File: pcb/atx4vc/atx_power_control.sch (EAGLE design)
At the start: 59 parts, among them IC2 REG1117, IC3 STM32F042F4, IC4 MY_7905DT, J1 ATX24RH, SW1 324_SW, SW2 324_SW, SW3 324_SW, SW4 324_SW, SW5 324_SW, SW7 324_SW, U1 USBC_16P, U2 USBC_16P

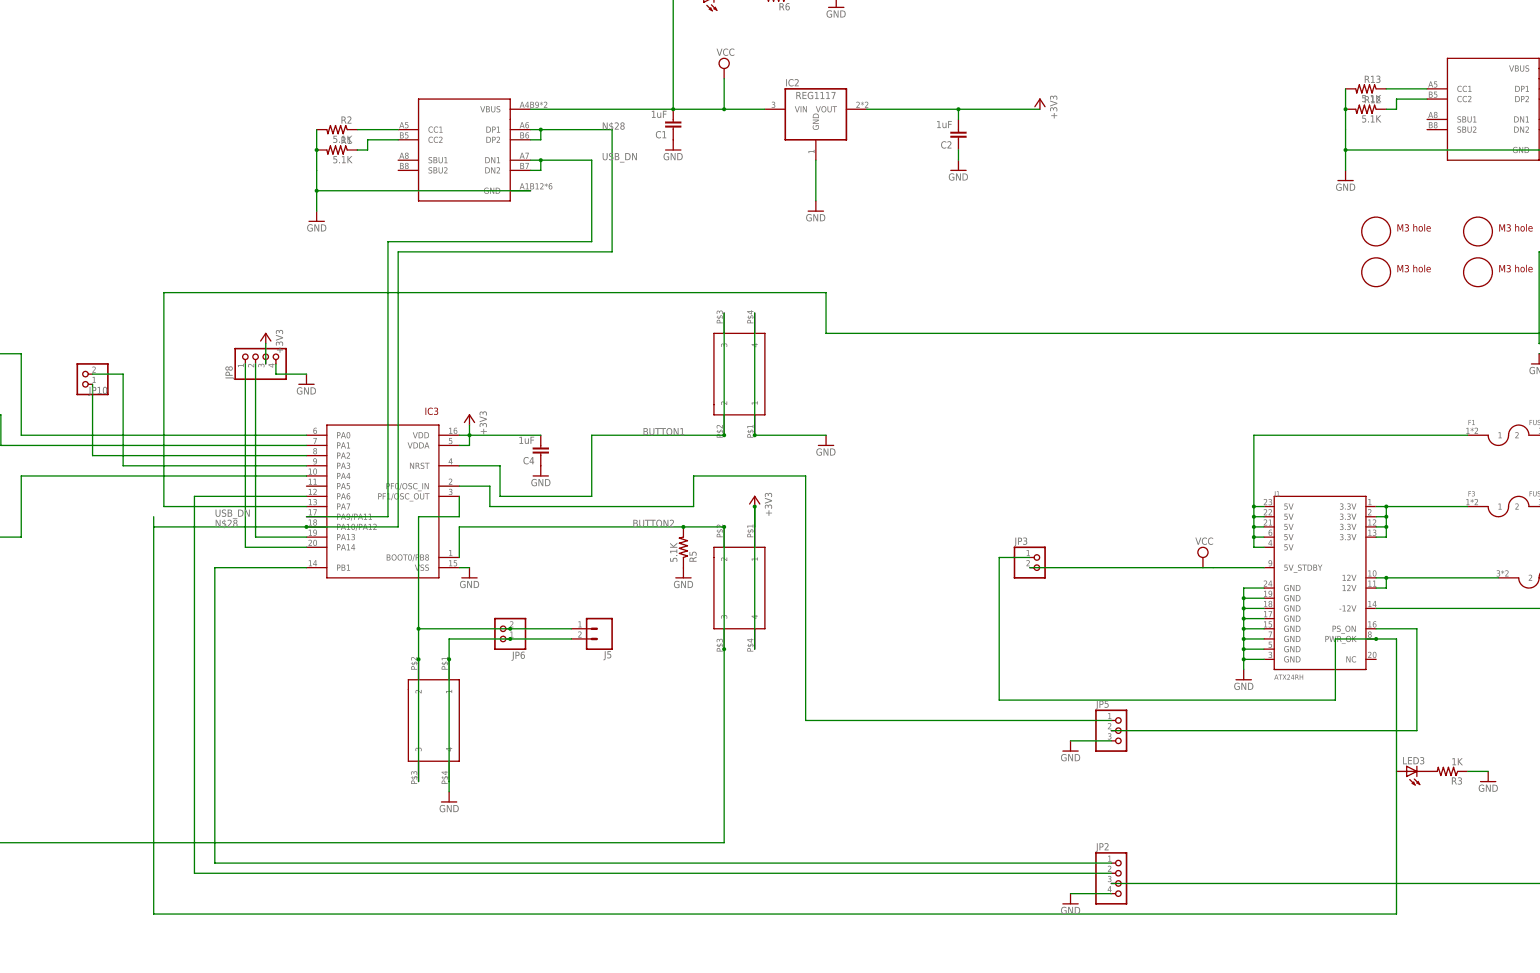
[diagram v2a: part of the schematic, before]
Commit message: added selector jumper for power-on detect
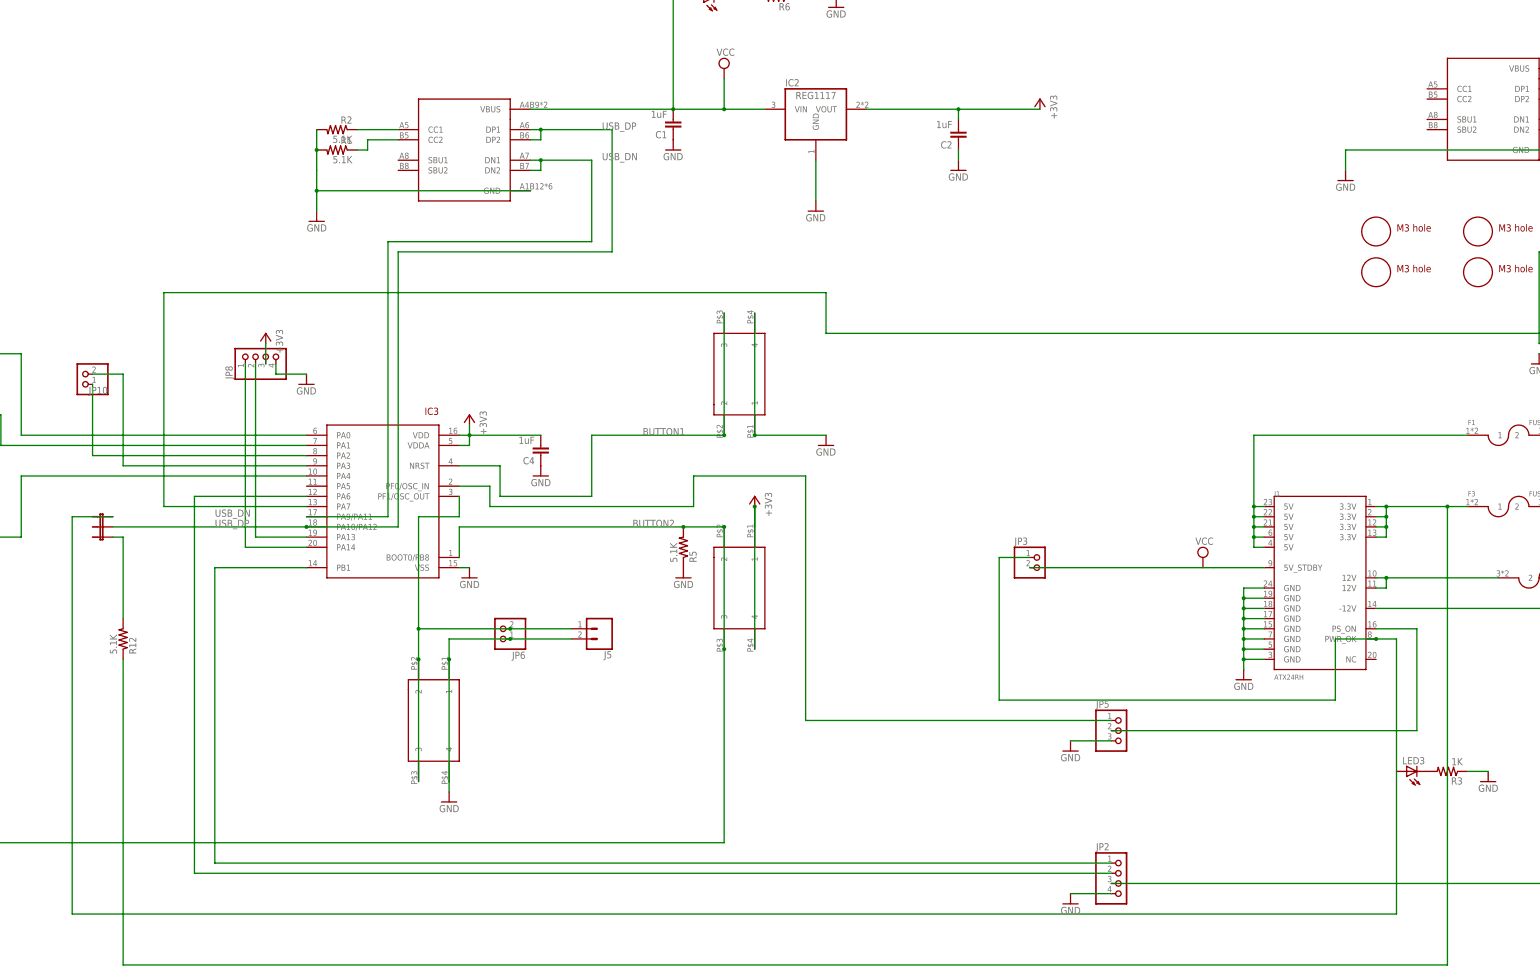
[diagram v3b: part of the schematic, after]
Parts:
- removed R13: 5.1K, joyAnalog:RESISTOR0805-RES
- added JP4: JUMPER-32-3, SparkFun-Retired:JUMPER-32-3
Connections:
- removed net N$28: IC3.PA10/PA12, J1.PWR_OK, JP3.1, LED3.A, U2.DP1, U2.DP2
- removed net N$32: R12.1, U1.CC2
- removed net N$34: R13.1, U1.CC1
- new net FFFF: J1.PWR_OK, JP3.1, JP4.1, LED3.A
- new net N$30: JP4.3, R12.2
- new net USB_DP: IC3.PA10/PA12, JP4.2, U2.DP1, U2.DP2
- net GND: no longer R12.2, R13.2
- net N$14: now also R12.1
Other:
- moved on the sheet: R12
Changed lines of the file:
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@@
 <part name="U1" library="my_usbc_16p" deviceset="USBC_16P" device=""/>
 <part name="GND31" library="supply1" deviceset="GND" device=""/>
+<part name="+3V3" library="supply1" library_urn="urn:adsk.eagle:library:371" deviceset="+3V3" device=""/>
+<part name="JP4" library="SparkFun-Retired" deviceset="JUMPER-3" device="2-3" value="JUMPER-32-3"/>
 <part name="R12" library="joyAnalog" deviceset="RESISTOR" device="0805-RES" value="5.1K"/>
-<part name="R13" library="joyAnalog" deviceset="RESISTOR" device="0805-RES" value="5.1K"/>
-<part name="+3V3" library="supply1" library_urn="urn:adsk.eagle:library:371" deviceset="+3V3" device=""/>
 </parts>
 <sheets>
@@
 <attribute name="VALUE" x="243.84" y="101.6" size="1.778" layer="96" rot="MR0"/>
 </instance>
-<instance part="R12" gate="G$1" x="246.38" y="121.92" smashed="yes" rot="MR0">
-<attribute name="NAME" x="250.19" y="123.4186" size="1.778" layer="95" rot="MR0"/>
-<attribute name="VALUE" x="250.19" y="118.618" size="1.778" layer="96" rot="MR0"/>
-<attribute name="NAME" x="250.19" y="123.4186" size="1.778" layer="95" rot="MR0"/>
-<attribute name="VALUE" x="250.19" y="118.618" size="1.778" layer="96" rot="MR0"/>
-</instance>
-<instance part="R13" gate="G$1" x="246.38" y="127" smashed="yes" rot="MR0">
-<attribute name="NAME" x="250.19" y="128.4986" size="1.778" layer="95" rot="MR0"/>
-<attribute name="VALUE" x="250.19" y="123.698" size="1.778" layer="96" rot="MR0"/>
-<attribute name="NAME" x="250.19" y="128.4986" size="1.778" layer="95" rot="MR0"/>
-<attribute name="VALUE" x="250.19" y="123.698" size="1.778" layer="96" rot="MR0"/>
-</instance>
 <instance part="+3V3" gate="G$1" x="-231.14" y="58.42" smashed="yes" rot="MR0">
 <attribute name="VALUE" x="-228.6" y="53.34" size="1.778" layer="96" rot="MR90"/>
+</instance>
+<instance part="JP4" gate="G$1" x="-68.58" y="20.32" smashed="yes" rot="MR270"/>
+<instance part="R12" gate="G$1" x="-63.5" y="-10.16" smashed="yes" rot="MR90">
+<attribute name="NAME" x="-62.0014" y="-13.97" size="1.778" layer="95" rot="MR90"/>
+<attribute name="VALUE" x="-66.802" y="-13.97" size="1.778" layer="96" rot="MR90"/>
+<attribute name="NAME" x="-62.0014" y="-13.97" size="1.778" layer="95" rot="MR90"/>
+<attribute name="VALUE" x="-66.802" y="-13.97" size="1.778" layer="96" rot="MR90"/>
 </instance>
 </instances>
@@
 <segment>
 <pinref part="GND31" gate="1" pin="GND"/>
-<wire x1="241.3" y1="116.84" x2="241.3" y2="111.76" width="0.1524" layer="91"/>
-<pinref part="R12" gate="G$1" pin="2"/>
 <wire x1="241.3" y1="111.76" x2="241.3" y2="106.68" width="0.1524" layer="91"/>
-<wire x1="241.3" y1="121.92" x2="241.3" y2="116.84" width="0.1524" layer="91"/>
-<junction x="241.3" y="121.92"/>
-<pinref part="R13" gate="G$1" pin="2"/>
-<wire x1="241.3" y1="127" x2="241.3" y2="121.92" width="0.1524" layer="91"/>
 <wire x1="294.64" y1="111.76" x2="241.3" y2="111.76" width="0.1524" layer="91"/>
-<junction x="241.3" y="111.76"/>
 <pinref part="U1" gate="G$1" pin="GND"/>
 </segment>
@@
 </segment>
 </net>
-<net name="N$28" class="0">
+<net name="FFFF" class="0">
 <segment>
 <pinref part="J1" gate="G$1" pin="PWR_OK"/>
@@
 <pinref part="JP3" gate="G$1" pin="1"/>
 <wire x1="154.94" y1="10.16" x2="162.56" y2="10.16" width="0.1524" layer="91"/>
-<pinref part="IC3" gate="G$1" pin="PA10/PA12"/>
-<wire x1="-17.78" y1="17.78" x2="-55.88" y2="17.78" width="0.1524" layer="91"/>
-<label x="-40.64" y="17.78" size="1.778" layer="95"/>
-<wire x1="-17.78" y1="17.78" x2="5.08" y2="17.78" width="0.1524" layer="91"/>
-<wire x1="5.08" y1="17.78" x2="5.08" y2="86.36" width="0.1524" layer="91"/>
-<junction x="-17.78" y="17.78"/>
-<wire x1="5.08" y1="86.36" x2="58.42" y2="86.36" width="0.1524" layer="91"/>
-<wire x1="58.42" y1="116.84" x2="40.64" y2="116.84" width="0.1524" layer="91"/>
-<label x="55.88" y="116.84" size="1.778" layer="95"/>
-<pinref part="U2" gate="G$1" pin="DP1"/>
-<wire x1="40.64" y1="116.84" x2="38.1" y2="116.84" width="0.1524" layer="91"/>
-<wire x1="40.64" y1="116.84" x2="40.64" y2="114.3" width="0.1524" layer="91"/>
-<junction x="40.64" y="116.84"/>
-<pinref part="U2" gate="G$1" pin="DP2"/>
-<wire x1="40.64" y1="114.3" x2="38.1" y2="114.3" width="0.1524" layer="91"/>
-<wire x1="58.42" y1="86.36" x2="58.42" y2="116.84" width="0.1524" layer="91"/>
 <wire x1="254" y1="-43.18" x2="254" y2="-78.74" width="0.1524" layer="91"/>
-<wire x1="254" y1="-78.74" x2="-55.88" y2="-78.74" width="0.1524" layer="91"/>
-<wire x1="-55.88" y1="-78.74" x2="-55.88" y2="17.78" width="0.1524" layer="91"/>
-<wire x1="-55.88" y1="20.32" x2="-55.88" y2="17.78" width="0.1524" layer="91"/>
+<wire x1="254" y1="-78.74" x2="-76.2" y2="-78.74" width="0.1524" layer="91"/>
+<wire x1="-76.2" y1="-78.74" x2="-76.2" y2="20.32" width="0.1524" layer="91"/>
+<pinref part="JP4" gate="G$1" pin="1"/>
+<wire x1="-66.04" y1="20.32" x2="-76.2" y2="20.32" width="0.1524" layer="91"/>
 </segment>
 </net>
@@
 <wire x1="-71.12" y1="35.56" x2="-71.12" y2="53.34" width="0.1524" layer="91"/>
 <pinref part="JP10" gate="G$1" pin="1"/>
-</segment>
-</net>
-<net name="N$32" class="0">
-<segment>
-<pinref part="R12" gate="G$1" pin="1"/>
-<wire x1="254" y1="121.92" x2="251.46" y2="121.92" width="0.1524" layer="91"/>
-<wire x1="261.62" y1="124.46" x2="254" y2="124.46" width="0.1524" layer="91"/>
-<wire x1="254" y1="124.46" x2="254" y2="121.92" width="0.1524" layer="91"/>
-<pinref part="U1" gate="G$1" pin="CC2"/>
-</segment>
-</net>
-<net name="N$34" class="0">
-<segment>
-<pinref part="R13" gate="G$1" pin="1"/>
-<wire x1="261.62" y1="127" x2="251.46" y2="127" width="0.1524" layer="91"/>
-<pinref part="U1" gate="G$1" pin="CC1"/>
 </segment>
 </net>
@@
 <pinref part="J1" gate="G$1" pin="3.3V@0"/>
 <wire x1="248.92" y1="22.86" x2="251.46" y2="22.86" width="0.1524" layer="91"/>
-<wire x1="251.46" y1="22.86" x2="271.78" y2="22.86" width="0.1524" layer="91"/>
+<wire x1="251.46" y1="22.86" x2="266.7" y2="22.86" width="0.1524" layer="91"/>
 <junction x="251.46" y="22.86"/>
+<wire x1="266.7" y1="22.86" x2="271.78" y2="22.86" width="0.1524" layer="91"/>
 <wire x1="251.46" y1="22.86" x2="251.46" y2="20.32" width="0.1524" layer="91"/>
 <pinref part="J1" gate="G$1" pin="3.3V@1"/>
@@
 <wire x1="251.46" y1="17.78" x2="251.46" y2="15.24" width="0.1524" layer="91"/>
 <wire x1="251.46" y1="15.24" x2="248.92" y2="15.24" width="0.1524" layer="91"/>
+<wire x1="266.7" y1="22.86" x2="266.7" y2="-91.44" width="0.1524" layer="91"/>
+<wire x1="266.7" y1="-91.44" x2="-63.5" y2="-91.44" width="0.1524" layer="91"/>
+<junction x="266.7" y="22.86"/>
+<wire x1="-63.5" y1="-91.44" x2="-63.5" y2="-15.24" width="0.1524" layer="91"/>
+<pinref part="R12" gate="G$1" pin="1"/>
 </segment>
 </net>
@@
 </segment>
 </net>
+<net name="USB_DP" class="0">
+<segment>
+<pinref part="U2" gate="G$1" pin="DP2"/>
+<wire x1="40.64" y1="114.3" x2="38.1" y2="114.3" width="0.1524" layer="91"/>
+<pinref part="U2" gate="G$1" pin="DP1"/>
+<wire x1="40.64" y1="116.84" x2="38.1" y2="116.84" width="0.1524" layer="91"/>
+<wire x1="40.64" y1="116.84" x2="40.64" y2="114.3" width="0.1524" layer="91"/>
+<junction x="40.64" y="116.84"/>
+<wire x1="58.42" y1="116.84" x2="40.64" y2="116.84" width="0.1524" layer="91"/>
+<wire x1="58.42" y1="86.36" x2="58.42" y2="116.84" width="0.1524" layer="91"/>
+<wire x1="5.08" y1="86.36" x2="58.42" y2="86.36" width="0.1524" layer="91"/>
+<wire x1="5.08" y1="17.78" x2="5.08" y2="86.36" width="0.1524" layer="91"/>
+<pinref part="IC3" gate="G$1" pin="PA10/PA12"/>
+<wire x1="-17.78" y1="17.78" x2="-66.04" y2="17.78" width="0.1524" layer="91"/>
+<wire x1="-17.78" y1="17.78" x2="5.08" y2="17.78" width="0.1524" layer="91"/>
+<junction x="-17.78" y="17.78"/>
+<label x="-40.64" y="17.78" size="1.778" layer="95"/>
+<label x="55.88" y="116.84" size="1.778" layer="95"/>
+<pinref part="JP4" gate="G$1" pin="2"/>
+</segment>
+</net>
+<net name="N$30" class="0">
+<segment>
+<pinref part="R12" gate="G$1" pin="2"/>
+<pinref part="JP4" gate="G$1" pin="3"/>
+<wire x1="-63.5" y1="-5.08" x2="-63.5" y2="15.24" width="0.1524" layer="91"/>
+<wire x1="-63.5" y1="15.24" x2="-66.04" y2="15.24" width="0.1524" layer="91"/>
+</segment>
+</net>

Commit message: adjusted power button and power LED
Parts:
- removed JP4: JUMPER-32-3, SparkFun-Retired:JUMPER-32-3
- added R13: 1K, SparkFun-Passives:RESISTOR0805-RES
- R12: value 5.1K -> 1K; device joyAnalog:RESISTOR0805-RES -> SparkFun-Passives:RESISTOR0805-RES
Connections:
- removed net FFFF: J1.PWR_OK, JP3.1, JP4.1, LED3.A
- removed net N$15: F1.2, J7.2, JP7.1, LED7.A, U1.VBUS
- net GND: now also R12.1, R13.1
- net N$14: no longer R12.1
- net N$17: now also R12.2
- net N$18: now also R13.2
- net N$19: no longer J8.2, JP1.1
- net N$30: now also F1.2, J7.2, J8.2, JP1.1, JP7.1, LED7.A, U1.VBUS; no longer JP4.3, R12.2
- net USB_DP: now also J1.PWR_OK, JP3.1, LED3.A; no longer JP4.2
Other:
- moved on the sheet: R11, R12
